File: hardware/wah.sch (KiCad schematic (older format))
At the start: 17 parts

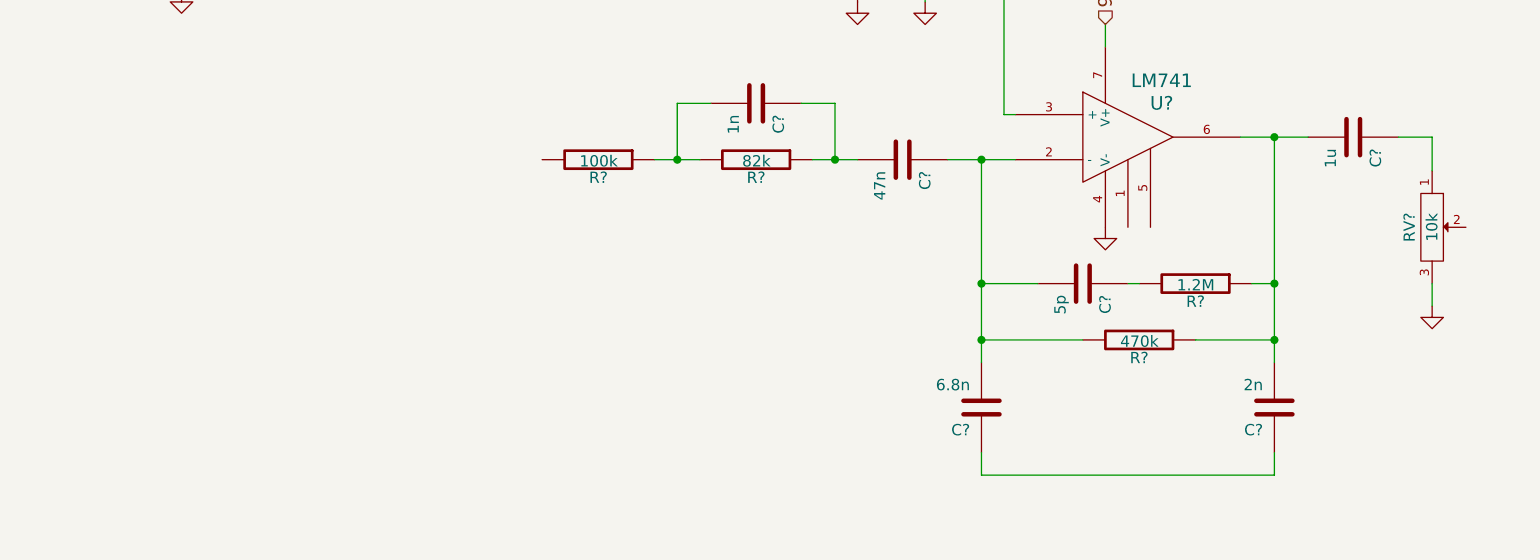
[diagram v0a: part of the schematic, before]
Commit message: Stub bypass subcircuit
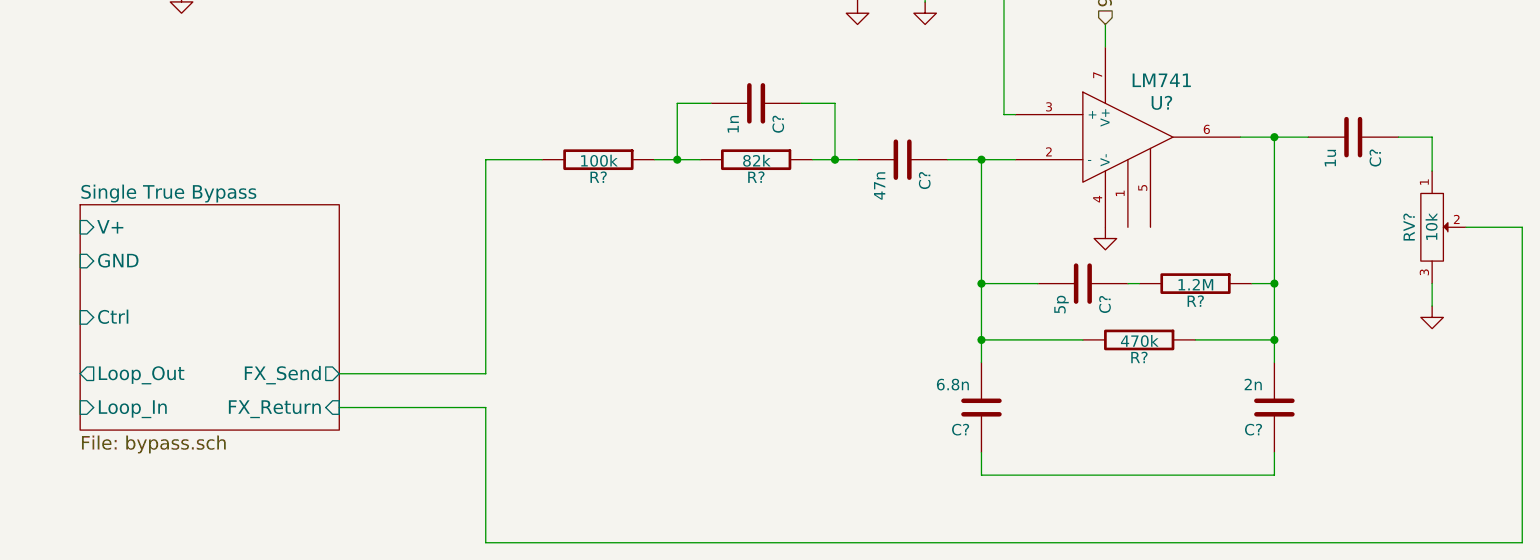
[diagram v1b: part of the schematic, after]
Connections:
- net Single True Bypass/FX_Send: now reaches R?.2
- net Single True Bypass/FX_Return: now reaches RV?.2
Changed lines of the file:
@@
 $Descr A4 11693 8268
 encoding utf-8
-Sheet 5 5
+Sheet 5 6
 Title ""
 Date ""
@@
 Wire Wire Line
 	7700 4050 7700 3950
+$Sheet
+S 1700 3600 1150 1000
+U 54D53732
+F0 "Single True Bypass" 60
+F1 "bypass.sch" 60
+F2 "Loop_In" I L 1700 4500 60
+F3 "Loop_Out" O L 1700 4350 60
+F4 "FX_Send" O R 2850 4350 60
+F5 "FX_Return" I R 2850 4500 60
+F6 "V+" I L 1700 3700 60
+F7 "GND" I L 1700 3850 60
+F8 "Ctrl" I L 1700 4100 60
+$EndSheet
+Wire Wire Line
+	2850 4350 3500 4350
+Wire Wire Line
+	3500 4350 3500 3400
+Wire Wire Line
+	3500 3400 3750 3400
+Wire Wire Line
+	2850 4500 3500 4500
+Wire Wire Line
+	3500 4500 3500 5100
+Wire Wire Line
+	3500 5100 8100 5100
+Wire Wire Line
+	8100 5100 8100 3700
+Wire Wire Line
+	8100 3700 7850 3700
 $EndSCHEMATC

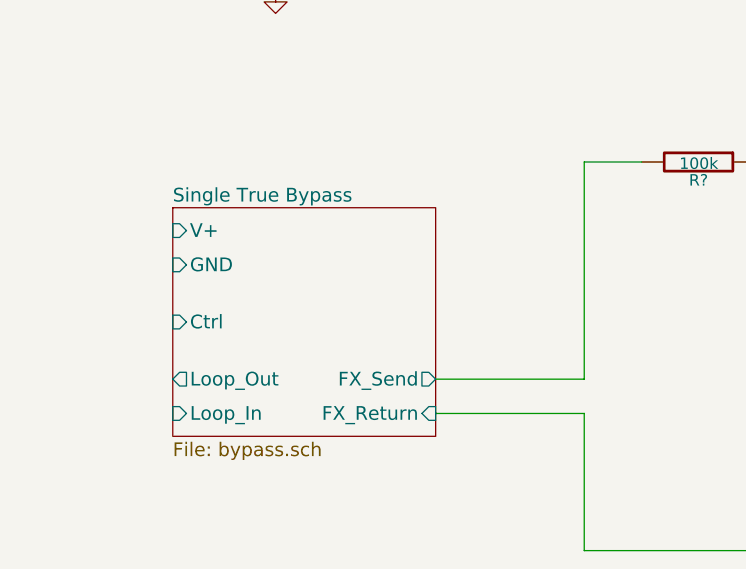
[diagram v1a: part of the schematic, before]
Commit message: Draw bypass circuit
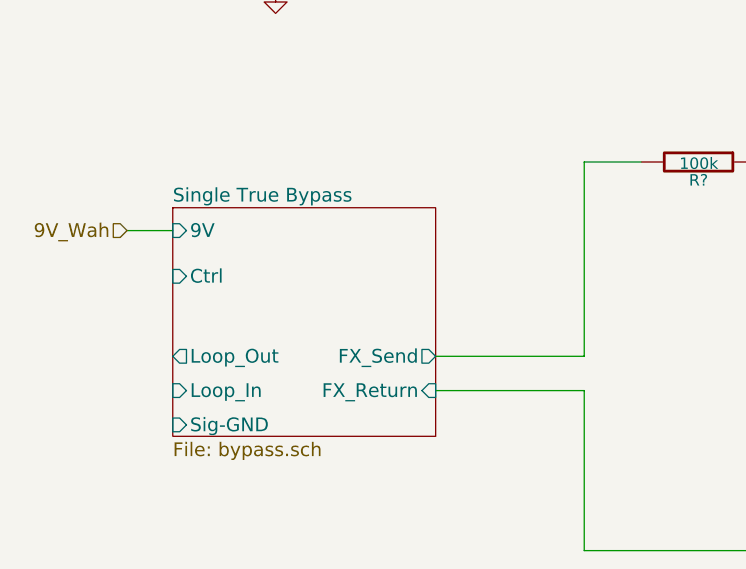
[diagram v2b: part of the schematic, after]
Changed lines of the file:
@@
 LIBS:contrib
 LIBS:valves
+LIBS:max1044
+LIBS:stacked_jack
+LIBS:relais_dpdt
 LIBS:uMIDI-FX-cache
 EELAYER 24 0
@@
 Text HLabel 1900 2000 0    60   Input ~ 0
 9V_Wah
-Text HLabel 1900 2600 0    60   Input ~ 0
-GND
 $Comp
 L R R?
@@
 	0    1    1    0
 $EndComp
-Wire Wire Line
-	4250 3400 4450 3400
-Wire Wire Line
-	4350 3400 4350 3150
-Wire Wire Line
-	4350 3150 4500 3150
-Connection ~ 4350 3400
 $Comp
 L C C?
@@
 	0    1    1    0
 $EndComp
-Wire Wire Line
-	4950 3400 5150 3400
-Wire Wire Line
-	5050 3400 5050 3150
-Wire Wire Line
-	5050 3150 4900 3150
-Connection ~ 5050 3400
 $Comp
 L LM741 U?
@@
 	1    0    0    -1
 $EndComp
-Wire Wire Line
-	5550 3400 5850 3400
 $Comp
 L GND #PWR?
@@
 	-1   0    0    1
 $EndComp
-Wire Wire Line
-	5050 2100 5800 2100
-Wire Wire Line
-	5800 2100 5800 3200
-Wire Wire Line
-	5800 3200 5850 3200
-Wire Wire Line
-	5150 2200 5150 2100
-Connection ~ 5150 2100
-Wire Wire Line
-	5450 2250 5450 2100
-Connection ~ 5450 2100
 $Comp
 L GND #PWR?
@@
 	1    0    0    -1
 $EndComp
-Wire Wire Line
-	5450 2700 5450 2650
 $Comp
 L C C?
@@
 	-1   0    0    1
 $EndComp
-Wire Wire Line
-	2300 2000 2300 2100
-Wire Wire Line
-	2000 2100 2000 2000
-Connection ~ 2000 2000
-Wire Wire Line
-	2000 2600 2000 2500
-Wire Wire Line
-	2300 2600 2300 2500
-Connection ~ 2000 2600
-Wire Wire Line
-	2150 2600 2150 2650
-Connection ~ 2150 2600
-Wire Wire Line
-	1900 2000 2300 2000
-Wire Wire Line
-	1900 2600 2300 2600
 Text HLabel 4450 2100 0    60   Input ~ 0
 9V_Wah
-Wire Wire Line
-	4450 2100 4550 2100
 Text HLabel 6250 2800 1    60   Input ~ 0
 9V_Wah
-Wire Wire Line
-	6250 2900 6250 2800
 $Comp
 L C C?
@@
 	0    1    1    0
 $EndComp
-Wire Wire Line
-	6350 3950 6400 3950
-Wire Wire Line
-	5700 4200 6150 4200
-Wire Wire Line
-	5700 3400 5700 4300
-Connection ~ 5700 3400
-Wire Wire Line
-	5700 3950 5950 3950
-Wire Wire Line
-	7000 4200 6650 4200
-Wire Wire Line
-	7000 3300 7000 4300
-Wire Wire Line
-	7000 3950 6900 3950
-Wire Wire Line
-	6850 3300 7150 3300
-Connection ~ 7000 3950
-Connection ~ 5700 3950
 $Comp
 L C C?
@@
 	-1   0    0    1
 $EndComp
-Connection ~ 7000 4200
-Connection ~ 5700 4200
-Wire Wire Line
-	5700 4700 5700 4800
-Wire Wire Line
-	5700 4800 7000 4800
-Wire Wire Line
-	7000 4800 7000 4700
 $Comp
 L C C?
@@
 	0    1    1    0
 $EndComp
-Connection ~ 7000 3300
 $Comp
 L POT RV?
@@
 	0    1    1    0
 $EndComp
-Wire Wire Line
-	7550 3300 7700 3300
-Wire Wire Line
-	7700 3300 7700 3450
 $Comp
 L GND #PWR?
@@
 	1    0    0    -1
 $EndComp
-Wire Wire Line
-	7700 4050 7700 3950
 $Sheet
 S 1700 3600 1150 1000
@@
 F0 "Single True Bypass" 60
 F1 "bypass.sch" 60
-F2 "Loop_In" I L 1700 4500 60
-F3 "Loop_Out" O L 1700 4350 60
-F4 "FX_Send" O R 2850 4350 60
-F5 "FX_Return" I R 2850 4500 60
-F6 "V+" I L 1700 3700 60
-F7 "GND" I L 1700 3850 60
-F8 "Ctrl" I L 1700 4100 60
+F2 "Loop_In" I L 1700 4400 60
+F3 "Loop_Out" O L 1700 4250 60
+F4 "FX_Send" O R 2850 4250 60
+F5 "FX_Return" I R 2850 4400 60
+F6 "9V" I L 1700 3700 60
+F7 "Ctrl" I L 1700 3900 60
+F8 "Sig-GND" I L 1700 4550 60
 $EndSheet
 Wire Wire Line
-	2850 4350 3500 4350
-Wire Wire Line
-	3500 4350 3500 3400
+	4250 3400 4450 3400
+Wire Wire Line
+	4350 3400 4350 3150
+Wire Wire Line
+	4350 3150 4500 3150
+Connection ~ 4350 3400
+Wire Wire Line
+	4950 3400 5150 3400
+Wire Wire Line
+	5050 3400 5050 3150
+Wire Wire Line
+	5050 3150 4900 3150
+Connection ~ 5050 3400
+Wire Wire Line
+	5550 3400 5850 3400
+Wire Wire Line
+	5050 2100 5800 2100
+Wire Wire Line
+	5800 2100 5800 3200
+Wire Wire Line
+	5800 3200 5850 3200
+Wire Wire Line
+	5150 2200 5150 2100
+Connection ~ 5150 2100
+Wire Wire Line
+	5450 2250 5450 2100
+Connection ~ 5450 2100
+Wire Wire Line
+	5450 2700 5450 2650
+Wire Wire Line
+	2300 2000 2300 2100
+Wire Wire Line
+	2000 2100 2000 2000
+Connection ~ 2000 2000
+Wire Wire Line
+	2000 2600 2000 2500
+Wire Wire Line
+	2300 2600 2300 2500
+Connection ~ 2000 2600
+Wire Wire Line
+	2150 2600 2150 2650
+Connection ~ 2150 2600
+Wire Wire Line
+	1900 2000 2300 2000
+Wire Wire Line
+	4450 2100 4550 2100
+Wire Wire Line
+	6250 2900 6250 2800
+Wire Wire Line
+	6350 3950 6400 3950
+Wire Wire Line
+	5700 4200 6150 4200
+Wire Wire Line
+	5700 3400 5700 4300
+Connection ~ 5700 3400
+Wire Wire Line
+	5700 3950 5950 3950
+Wire Wire Line
+	7000 4200 6650 4200
+Wire Wire Line
+	7000 3300 7000 4300
+Wire Wire Line
+	7000 3950 6900 3950
+Wire Wire Line
+	6850 3300 7150 3300
+Connection ~ 7000 3950
+Connection ~ 5700 3950
+Connection ~ 7000 4200
+Connection ~ 5700 4200
+Wire Wire Line
+	5700 4700 5700 4800
+Wire Wire Line
+	5700 4800 7000 4800
+Wire Wire Line
+	7000 4800 7000 4700
+Connection ~ 7000 3300
+Wire Wire Line
+	7550 3300 7700 3300
+Wire Wire Line
+	7700 3300 7700 3450
+Wire Wire Line
+	7700 4050 7700 3950
 Wire Wire Line
 	3500 3400 3750 3400
 Wire Wire Line
-	2850 4500 3500 4500
-Wire Wire Line
-	3500 4500 3500 5100
+	3500 4400 3500 5100
 Wire Wire Line
 	3500 5100 8100 5100
@@
 Wire Wire Line
 	8100 3700 7850 3700
+Wire Wire Line
+	2850 4400 3500 4400
+Wire Wire Line
+	2850 4250 3500 4250
+Wire Wire Line
+	3500 4250 3500 3400
+Text HLabel 1500 3700 0    60   Input ~ 0
+9V_Wah
+Wire Wire Line
+	1500 3700 1700 3700
+Wire Wire Line
+	1900 2600 2300 2600
+Text HLabel 1900 2600 0    60   Input ~ 0
+GND
 $EndSCHEMATC

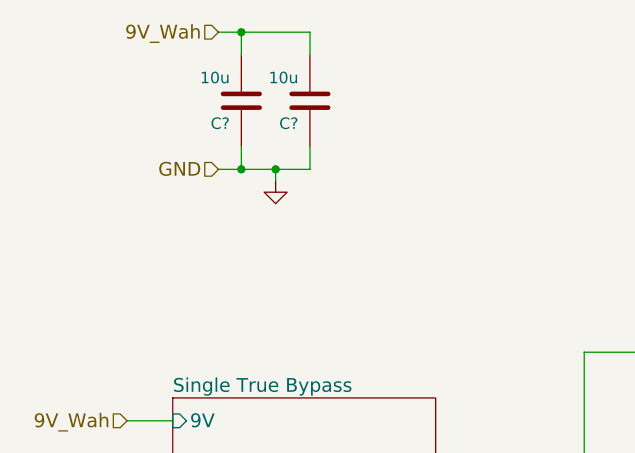
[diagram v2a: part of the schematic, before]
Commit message: Combine bypass and stacked jack to looper circuit
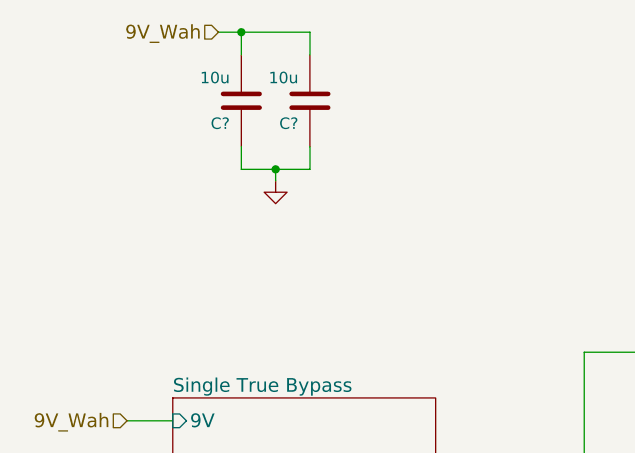
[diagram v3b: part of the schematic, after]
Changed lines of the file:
@@
 $Descr A4 11693 8268
 encoding utf-8
-Sheet 5 6
+Sheet 12 19
 Title ""
 Date ""
@@
 Wire Wire Line
 	2300 2600 2300 2500
-Connection ~ 2000 2600
 Wire Wire Line
 	2150 2600 2150 2650
@@
 	1500 3700 1700 3700
 Wire Wire Line
-	1900 2600 2300 2600
-Text HLabel 1900 2600 0    60   Input ~ 0
-GND
+	2000 2600 2300 2600
 $EndSCHEMATC

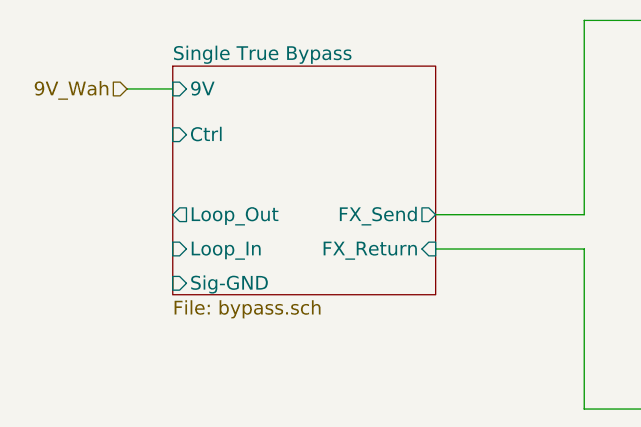
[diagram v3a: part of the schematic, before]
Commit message: Replace Sig-GND label by global GNDA label
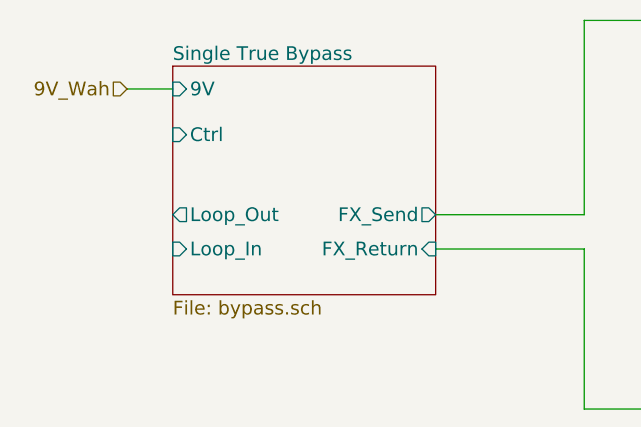
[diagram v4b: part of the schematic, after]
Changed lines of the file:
@@
 $Descr A4 11693 8268
 encoding utf-8
-Sheet 12 19
+Sheet 18 19
 Title ""
 Date ""
@@
 F6 "9V" I L 1700 3700 60
 F7 "Ctrl" I L 1700 3900 60
-F8 "Sig-GND" I L 1700 4550 60
 $EndSheet
 Wire Wire Line
